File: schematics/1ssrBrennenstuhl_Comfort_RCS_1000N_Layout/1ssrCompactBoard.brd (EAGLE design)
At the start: 46 x 47 mm, 20 parts, among them K1 AQG12105

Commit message: board work in progress
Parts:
- moved OUT 3.59 mm to (31.4, 5.08)
- moved N 1.27 mm to (15.3, 3.81)
- moved C1 0.56 mm to (2.29, 12.3)
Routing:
- net OUT: track 10.0 -> 6.45 mm
- net GND: track 97.5 -> 98.2 mm
- net NEUTRAL: track 19.1 -> 18.5 mm
- net 5V: track 57.7 -> 57.1 mm
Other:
- outline, holes or cut-outs redrawn
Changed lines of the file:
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@@
 <setting verticaltext="up"/>
 </settings>
-<grid distance="9.84251969" unitdist="mil" unit="mil" style="lines" multiple="1" display="yes" altdistance="0.025" altunitdist="inch" altunit="inch"/>
+<grid distance="0.05" unitdist="inch" unit="inch" style="lines" multiple="1" display="no" altdistance="0.025" altunitdist="inch" altunit="inch"/>
 <layers>
 <layer number="1" name="Top" color="4" fill="1" visible="yes" active="yes"/>
@@
 <board>
 <plain>
-<wire x1="0" y1="0" x2="46" y2="0" width="0" layer="20"/>
+<wire x1="0" y1="0" x2="16" y2="0" width="0" layer="20"/>
+<wire x1="16" y1="0" x2="19" y2="2" width="0" layer="20"/>
+<wire x1="19" y1="2" x2="30" y2="2" width="0" layer="20"/>
+<wire x1="30" y1="2" x2="33" y2="0" width="0" layer="20"/>
+<wire x1="33" y1="0" x2="46" y2="0" width="0" layer="20"/>
 <wire x1="46" y1="0" x2="46" y2="47" width="0" layer="20"/>
 <wire x1="46" y1="47" x2="0" y2="47" width="0" layer="20"/>
@@
 </autorouter>
 <elements>
-<element name="C1" library="SparkFun-Capacitors" package="0603-CAP" value="0.1uF" x="2.54" y="11.76" rot="MR270">
-<attribute name="PROD_ID" value="CAP-08604" x="2.54" y="11.76" size="1.778" layer="28" rot="MR270" display="off"/>
+<element name="C1" library="SparkFun-Capacitors" package="0603-CAP" value="0.1uF" x="2.29" y="12.26" rot="MR270">
+<attribute name="PROD_ID" value="CAP-08604" x="2.29" y="12.26" size="1.778" layer="28" rot="MR270" display="off"/>
 </element>
 <element name="C2" library="SparkFun-Capacitors" package="0603-CAP" value="0.1uF" x="6.5" y="13" rot="MR270">
@@
 <attribute name="VALUE" x="27.54" y="36.385" size="1.27" layer="28" rot="MR270"/>
 </element>
-<element name="N" library="wirepad" package="3,81/1,1" value="" x="15.32" y="2.54" smashed="yes">
-<attribute name="NAME" x="15.915" y="4.826" size="1.27" layer="25" ratio="10" rot="MR0"/>
-<attribute name="VALUE" x="15.32" y="3.74" size="0.0254" layer="27"/>
+<element name="N" library="wirepad" package="3,81/1,1" value="" x="15.32" y="3.81" smashed="yes">
+<attribute name="NAME" x="15.915" y="6.096" size="1.27" layer="25" ratio="10" rot="MR0"/>
+<attribute name="VALUE" x="15.32" y="5.01" size="0.0254" layer="27"/>
 </element>
 <element name="L" library="wirepad" package="3,81/1,1" value="" x="38.46" y="2.54" smashed="yes">
@@
 <attribute name="VALUE" x="38.46" y="3.74" size="0.0254" layer="27"/>
 </element>
-<element name="OUT" library="wirepad" package="3,81/1,1" value="" x="28.87" y="2.54" smashed="yes">
-<attribute name="NAME" x="27.965" y="5.076" size="1.27" layer="26" ratio="10" rot="MR0" align="bottom-center"/>
-<attribute name="VALUE" x="28.87" y="3.74" size="0.0254" layer="27"/>
+<element name="OUT" library="wirepad" package="3,81/1,1" value="" x="31.41" y="5.08" smashed="yes">
+<attribute name="NAME" x="30.505" y="7.616" size="1.27" layer="26" ratio="10" rot="MR0" align="bottom-center"/>
+<attribute name="VALUE" x="31.41" y="6.28" size="0.0254" layer="27"/>
 </element>
 <element name="D2" library="SparkFun-LED" package="LED-0603" value="" x="32.5" y="32" rot="MR0"/>
@@
 <contactref element="MDL1" pad="9"/>
 <contactref element="J1" pad="1"/>
-<wire x1="2.54" y1="10.91" x2="6.5" y2="12.15" width="0.4064" layer="16"/>
+<wire x1="2.29" y1="11.41" x2="6.5" y2="12.15" width="0.4064" layer="16"/>
 <wire x1="6.5" y1="12.15" x2="8.529575" y2="12.22" width="0.4064" layer="16"/>
 <wire x1="8.529575" y1="12.22" x2="8.9785875" y2="12.4059875" width="0.4064" layer="16" curve="45"/>
@@
 <wire x1="6" y1="37.486975" x2="5.8140125" y2="37.9359875" width="0.4064" layer="1" curve="45"/>
 <wire x1="5.8140125" y1="37.9359875" x2="3" y2="40.75" width="0.4064" layer="1"/>
-<wire x1="2.34" y1="7.1" x2="2.59" y2="10.789290625" width="0.4064" layer="16"/>
-<wire x1="2.59" y1="10.789290625" x2="2.54" y2="10.91" width="0.4064" layer="16" curve="45"/>
+<wire x1="2.34" y1="7.1" x2="2.29" y2="7.1" width="0.4064" layer="16"/>
+<wire x1="2.29" y1="7.1" x2="2.29" y2="11.41" width="0.4064" layer="16"/>
 </signal>
 <signal name="5V">
@@
 <contactref element="D1" pad="C"/>
 <contactref element="R4" pad="2"/>
-<wire x1="2.54" y1="12.61" x2="2.59" y2="12.61" width="0.4064" layer="16"/>
-<wire x1="2.59" y1="12.61" x2="2.34" y2="22.5" width="0.4064" layer="16"/>
 <wire x1="32.5" y1="27.15" x2="35.376975" y2="27.15" width="0.4064" layer="16"/>
 <wire x1="35.376975" y1="27.15" x2="35.8259875" y2="27.3359875" width="0.4064" layer="16" curve="45"/>
@@
 <wire x1="30.336975" y1="25.25" x2="30.7859875" y2="25.4359875" width="0.4064" layer="16" curve="45"/>
 <wire x1="30.7859875" y1="25.4359875" x2="32.5" y2="27.15" width="0.4064" layer="16"/>
+<wire x1="2.34" y1="22.5" x2="2.29" y2="13.11" width="0.4064" layer="16"/>
 </signal>
 <signal name="GPIO0">
@@
 <contactref element="N" pad="1"/>
 <contactref element="U$4" pad="AC1"/>
-<wire x1="31.74" y1="12.3" x2="15.32" y2="2.54" width="2.54" layer="1"/>
+<wire x1="31.74" y1="12.3" x2="15.32" y2="3.81" width="2.54" layer="1"/>
 </signal>
 <signal name="LINE" class="1">
@@
 <contactref element="FUSE" pad="1"/>
 <wire x1="38.46" y1="2.54" x2="42.69" y2="6.57" width="3.81" layer="1"/>
-<wire x1="42.69" y1="6.57" x2="42.75" y2="12.5" width="0" layer="19" extent="1-16"/>
-<wire x1="42.75" y1="12.5" x2="42.69" y2="6.57" width="0" layer="19" extent="1-16"/>
 </signal>
 <signal name="OUT" class="1">
 <contactref element="OUT" pad="1"/>
 <contactref element="K1" pad="O2"/>
-<wire x1="28.87" y1="2.54" x2="34.75" y2="8" width="2.54" layer="16"/>
+<wire x1="31.41" y1="5.08" x2="34.75" y2="8" width="2.54" layer="16"/>
 <wire x1="34.75" y1="8" x2="35.91" y2="9.64" width="2.05" layer="16"/>
 </signal>

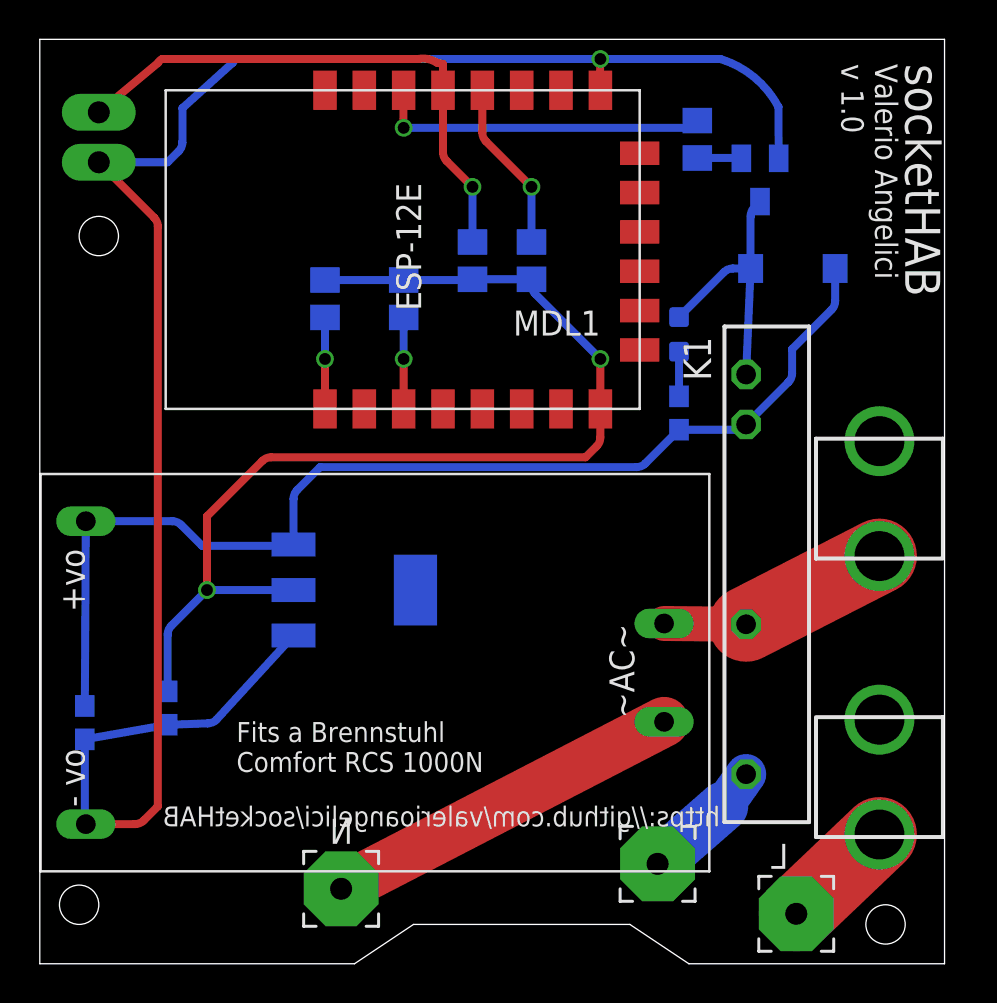
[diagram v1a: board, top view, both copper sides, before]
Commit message: added missing connection on pin gpio15
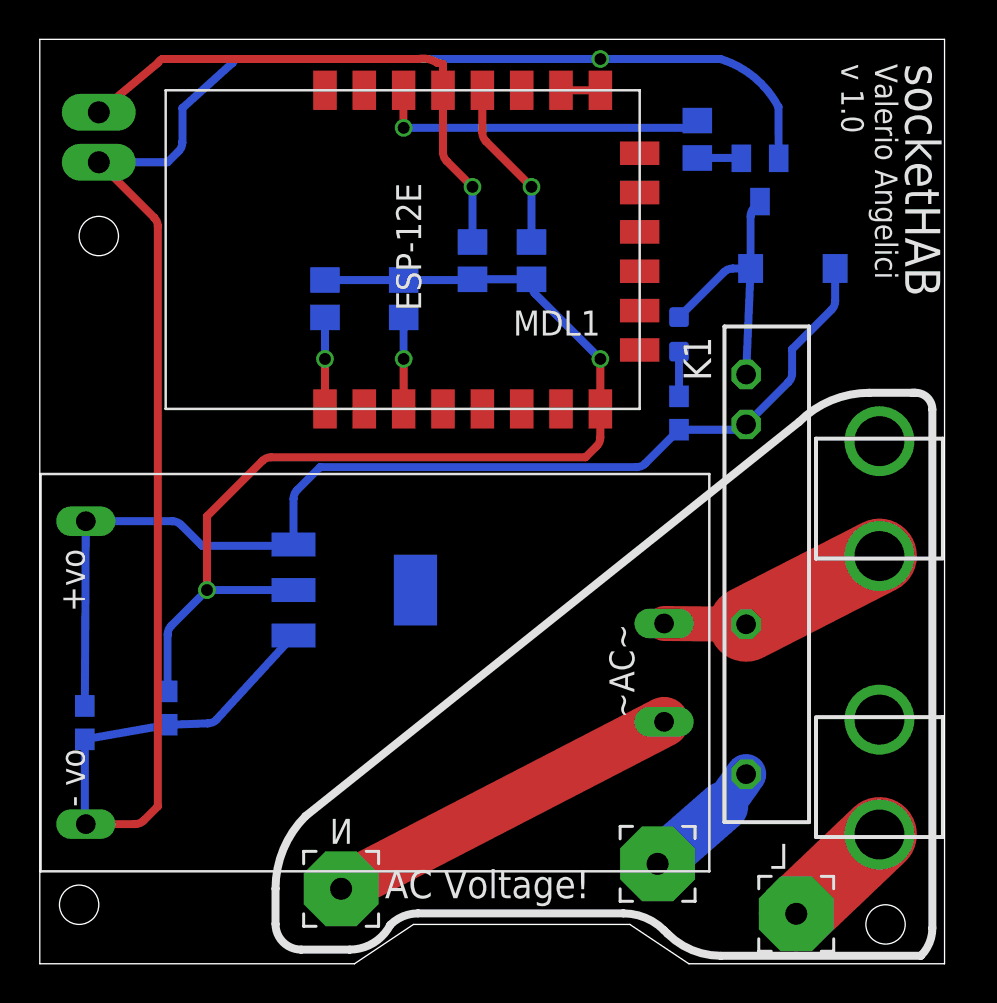
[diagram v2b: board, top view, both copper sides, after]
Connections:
- net GND: now also MDL1.10
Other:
- board text added: "AC Voltage!"
- board text added: "Warning AC Voltage!"
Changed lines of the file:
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@@
 <?xml version="1.0" encoding="utf-8"?>
 <!DOCTYPE eagle SYSTEM "eagle.dtd">
-<eagle version="7.5.0">
+<eagle version="7.6.0">
 <drawing>
 <settings>
@@
 <layer number="27" name="tValues" color="7" fill="1" visible="no" active="yes"/>
 <layer number="28" name="bValues" color="7" fill="1" visible="no" active="yes"/>
-<layer number="29" name="tStop" color="7" fill="3" visible="no" active="yes"/>
-<layer number="30" name="bStop" color="7" fill="6" visible="no" active="yes"/>
-<layer number="31" name="tCream" color="7" fill="4" visible="no" active="yes"/>
-<layer number="32" name="bCream" color="7" fill="5" visible="no" active="yes"/>
-<layer number="33" name="tFinish" color="6" fill="3" visible="no" active="yes"/>
-<layer number="34" name="bFinish" color="6" fill="6" visible="no" active="yes"/>
-<layer number="35" name="tGlue" color="7" fill="4" visible="no" active="yes"/>
-<layer number="36" name="bGlue" color="7" fill="5" visible="no" active="yes"/>
-<layer number="37" name="tTest" color="7" fill="1" visible="no" active="yes"/>
-<layer number="38" name="bTest" color="7" fill="1" visible="no" active="yes"/>
+<layer number="29" name="tStop" color="7" fill="3" visible="yes" active="yes"/>
+<layer number="30" name="bStop" color="7" fill="6" visible="yes" active="yes"/>
+<layer number="31" name="tCream" color="7" fill="4" visible="yes" active="yes"/>
+<layer number="32" name="bCream" color="7" fill="5" visible="yes" active="yes"/>
+<layer number="33" name="tFinish" color="6" fill="3" visible="yes" active="yes"/>
+<layer number="34" name="bFinish" color="6" fill="6" visible="yes" active="yes"/>
+<layer number="35" name="tGlue" color="7" fill="4" visible="yes" active="yes"/>
+<layer number="36" name="bGlue" color="7" fill="5" visible="yes" active="yes"/>
+<layer number="37" name="tTest" color="7" fill="1" visible="yes" active="yes"/>
+<layer number="38" name="bTest" color="7" fill="1" visible="yes" active="yes"/>
 <layer number="39" name="tKeepout" color="4" fill="11" visible="yes" active="yes"/>
 <layer number="40" name="bKeepout" color="1" fill="11" visible="yes" active="yes"/>
@@
 <layer number="42" name="bRestrict" color="1" fill="10" visible="yes" active="yes"/>
 <layer number="43" name="vRestrict" color="2" fill="10" visible="yes" active="yes"/>
-<layer number="44" name="Drills" color="7" fill="1" visible="no" active="yes"/>
+<layer number="44" name="Drills" color="7" fill="1" visible="yes" active="yes"/>
 <layer number="45" name="Holes" color="7" fill="1" visible="yes" active="yes"/>
-<layer number="46" name="Milling" color="3" fill="1" visible="no" active="yes"/>
-<layer number="47" name="Measures" color="7" fill="1" visible="no" active="yes"/>
+<layer number="46" name="Milling" color="3" fill="1" visible="yes" active="yes"/>
+<layer number="47" name="Measures" color="7" fill="1" visible="yes" active="yes"/>
 <layer number="48" name="Document" color="7" fill="1" visible="yes" active="yes"/>
 <layer number="49" name="Reference" color="7" fill="1" visible="yes" active="yes"/>
@@
 <text x="40.75" y="45.75" size="1.143" layer="112" rot="SR270">Valerio Angelici
 v 1.0</text>
-<text x="6.25" y="8" size="1.016" layer="121" distance="56" rot="MR180">https://github.com/valerioangelici/socketHAB</text>
+<text x="6.25" y="8" size="1.016" layer="122" distance="56" rot="MR180">https://github.com/valerioangelici/socketHAB</text>
 <text x="40.75" y="30.5" size="1.143" layer="122" rot="SMR90">Valerio Angelici
 v 1.0</text>
-<text x="10" y="9.75" size="1.016" layer="112" rot="SR0">Fits a Brennstuhl
-Comfort RCS 1000N</text>
 <text x="23.25" y="9.75" size="1.016" layer="122" rot="SMR0">Fits a Brennstuhl
 Comfort RCS 1000N</text>
+<wire x1="44.483065625" y1="29.02995" x2="42.183034375" y2="29.02995" width="0.4064" layer="112"/>
+<wire x1="42.183034375" y1="29.02995" x2="38.6028625" y2="27.54699375" width="0.4064" layer="112" curve="45"/>
+<wire x1="38.6028625" y1="27.54699375" x2="13.511003125" y2="7.504646875" width="0.4064" layer="112"/>
+<wire x1="13.511003125" y1="7.504646875" x2="11.984840625" y2="3.820165625" width="0.4064" layer="112" curve="45"/>
+<wire x1="11.984840625" y1="3.820165625" x2="11.984840625" y2="2.022209375" width="0.4064" layer="112"/>
+<wire x1="11.984840625" y1="2.022209375" x2="13.288040625" y2="0.719009375" width="0.4064" layer="112" curve="90"/>
+<wire x1="13.288040625" y1="0.719009375" x2="15.755353125" y2="0.719009375" width="0.4064" layer="112"/>
+<wire x1="15.755353125" y1="0.719009375" x2="17.820159375" y2="1.977271875" width="0.4064" layer="112" curve="62.715019"/>
+<wire x1="17.820159375" y1="1.977271875" x2="19.230528125" y2="2.561465625" width="0.4064" layer="112" curve="-45"/>
+<wire x1="19.230528125" y1="2.561465625" x2="29.6703375" y2="2.561465625" width="0.4064" layer="112"/>
+<wire x1="29.6703375" y1="2.561465625" x2="31.737265625" y2="1.705315625" width="0.4064" layer="112" curve="-45"/>
+<wire x1="31.737265625" y1="1.705315625" x2="31.914690625" y2="1.527890625" width="0.4064" layer="112"/>
+<wire x1="31.914690625" y1="1.527890625" x2="34.6269375" y2="0.404440625" width="0.4064" layer="112" curve="45"/>
+<wire x1="34.6269375" y1="0.404440625" x2="44.797275" y2="0.404440625" width="0.4064" layer="112"/>
+<wire x1="44.797275" y1="0.404440625" x2="45.38080625" y2="1.813209375" width="0.4064" layer="112" curve="45"/>
+<wire x1="45.38080625" y1="1.813209375" x2="45.38080625" y2="28.176128125" width="0.4064" layer="112"/>
+<wire x1="45.38080625" y1="28.176128125" x2="44.526575" y2="29.030359375" width="0.4064" layer="112" curve="90"/>
+<wire x1="44.526575" y1="29.030359375" x2="44.334346875" y2="29.030359375" width="0.4064" layer="112"/>
+<text x="42.979346875" y="14.48208125" size="1.4224" layer="122" rot="MR0">Warning AC Voltage!</text>
+<text x="17.543353125" y="3.330503125" size="1.4224" layer="112">AC Voltage!</text>
+<wire x1="44.50925" y1="29.128990625" x2="42.20921875" y2="29.128990625" width="0.4064" layer="122"/>
+<wire x1="42.20921875" y1="29.128990625" x2="38.629046875" y2="27.646034375" width="0.4064" layer="122" curve="45"/>
+<wire x1="38.629046875" y1="27.646034375" x2="13.5371875" y2="7.6036875" width="0.4064" layer="122"/>
+<wire x1="13.5371875" y1="7.6036875" x2="12.011025" y2="3.91920625" width="0.4064" layer="122" curve="45"/>
+<wire x1="12.011025" y1="3.91920625" x2="12.011025" y2="2.12125" width="0.4064" layer="122"/>
+<wire x1="12.011025" y1="2.12125" x2="13.314225" y2="0.81805" width="0.4064" layer="122" curve="90"/>
+<wire x1="13.314225" y1="0.81805" x2="15.7815375" y2="0.81805" width="0.4064" layer="122"/>
+<wire x1="15.7815375" y1="0.81805" x2="17.84634375" y2="2.0763125" width="0.4064" layer="122" curve="62.715019"/>
+<wire x1="17.84634375" y1="2.0763125" x2="19.2567125" y2="2.66050625" width="0.4064" layer="122" curve="-45"/>
+<wire x1="19.2567125" y1="2.66050625" x2="29.696521875" y2="2.66050625" width="0.4064" layer="122"/>
+<wire x1="29.696521875" y1="2.66050625" x2="31.76345" y2="1.80435625" width="0.4064" layer="122" curve="-45"/>
+<wire x1="31.940875" y1="1.62693125" x2="34.653121875" y2="0.50348125" width="0.4064" layer="122" curve="45"/>
+<wire x1="34.653121875" y1="0.50348125" x2="44.823459375" y2="0.50348125" width="0.4064" layer="122"/>
+<wire x1="44.823459375" y1="0.50348125" x2="45.406990625" y2="1.91225" width="0.4064" layer="122" curve="45"/>
+<wire x1="45.406990625" y1="1.91225" x2="45.406990625" y2="28.27516875" width="0.4064" layer="122"/>
+<wire x1="45.406990625" y1="28.27516875" x2="44.552759375" y2="29.1294" width="0.4064" layer="122" curve="90"/>
+<wire x1="44.552759375" y1="29.1294" x2="44.36053125" y2="29.1294" width="0.4064" layer="122"/>
 </plain>
 <attributes>
@@
 </element>
 <element name="MDL1" library="ESP8266-ESP12E" package="ESP8266-ESP12E" value="" x="30.5" y="28.21" rot="R90"/>
-<element name="Q1" library="semicon-smd-ipc" package="SOT23" value="" x="36.62" y="39.85" rot="MR180"/>
+<element name="Q1" library="semicon-smd-ipc" package="SOT23" value="" x="36.62" y="39.85" smashed="yes" rot="MR180">
+<attribute name="NAME" x="38.525" y="40.485" size="1.27" layer="26" rot="MR180"/>
+<attribute name="VALUE" x="34.715" y="43.025" size="1.27" layer="28" rot="MR180"/>
+</element>
 <element name="R2" library="resistor" package="R0805" value="10K" x="18.5" y="33.81" rot="MR270"/>
 <element name="R3" library="resistor" package="R0805" value="10K" x="33.43" y="41.92" rot="MR270"/>
@@
 <contactref element="C2" pad="2"/>
 <contactref element="Q1" pad="2"/>
-<contactref element="MDL1" pad="9"/>
 <contactref element="J1" pad="1"/>
 <wire x1="2.29" y1="11.41" x2="6.5" y2="12.15" width="0.4064" layer="16"/>
@@
 <wire x1="8.529575" y1="12.22" x2="8.9785875" y2="12.4059875" width="0.4064" layer="16" curve="45"/>
 <wire x1="8.9785875" y1="12.4059875" x2="12.9012" y2="16.6886" width="0.4064" layer="16"/>
-<wire x1="28.5" y1="44.41" x2="28.48" y2="46.201715625" width="0.4064" layer="1"/>
 <wire x1="28.48" y1="46.201715625" x2="28.5" y2="46" width="0.4064" layer="1" curve="-45"/>
 <via x="28.5" y="46" extent="1-16" drill="0.6"/>
@@
 <wire x1="2.34" y1="7.1" x2="2.29" y2="7.1" width="0.4064" layer="16"/>
 <wire x1="2.29" y1="7.1" x2="2.29" y2="11.41" width="0.4064" layer="16"/>
+<contactref element="MDL1" pad="10"/>
+<contactref element="MDL1" pad="9"/>
+<wire x1="28.5" y1="46" x2="28.5" y2="44.41" width="0" layer="19" extent="1-1"/>
+<wire x1="26.5" y1="44.41" x2="28.5" y2="44.41" width="0.4064" layer="1"/>
 </signal>
 <signal name="5V">
